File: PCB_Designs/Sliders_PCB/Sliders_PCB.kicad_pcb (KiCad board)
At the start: 2 copper layers, 67.1 x 80.5 mm, 6 parts, among them P1 CONN_01X06

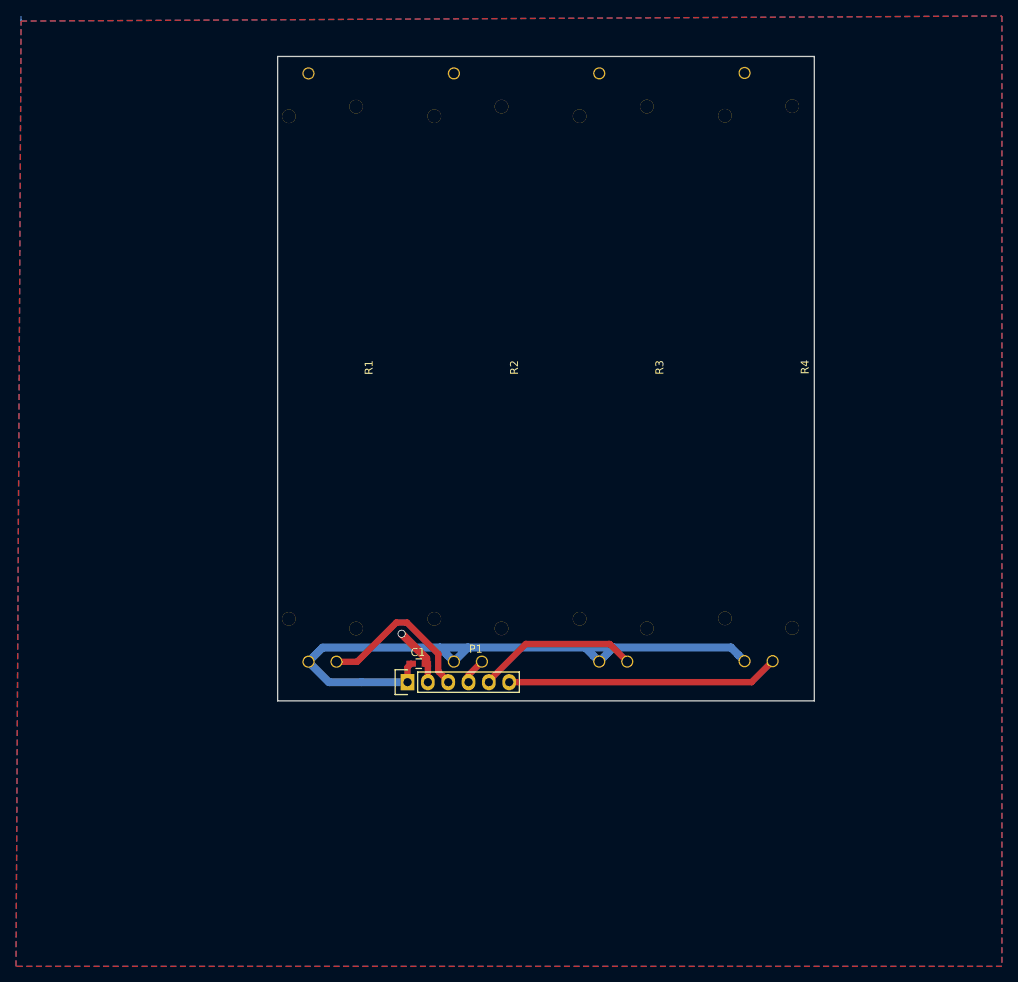
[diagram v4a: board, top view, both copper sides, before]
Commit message: Completed all Circuits for evaluation
* All board-to-board connectors now Multicomp 02X05
* Mounting holes for all PCB
* Vias at all groundpins
* Minor other changes
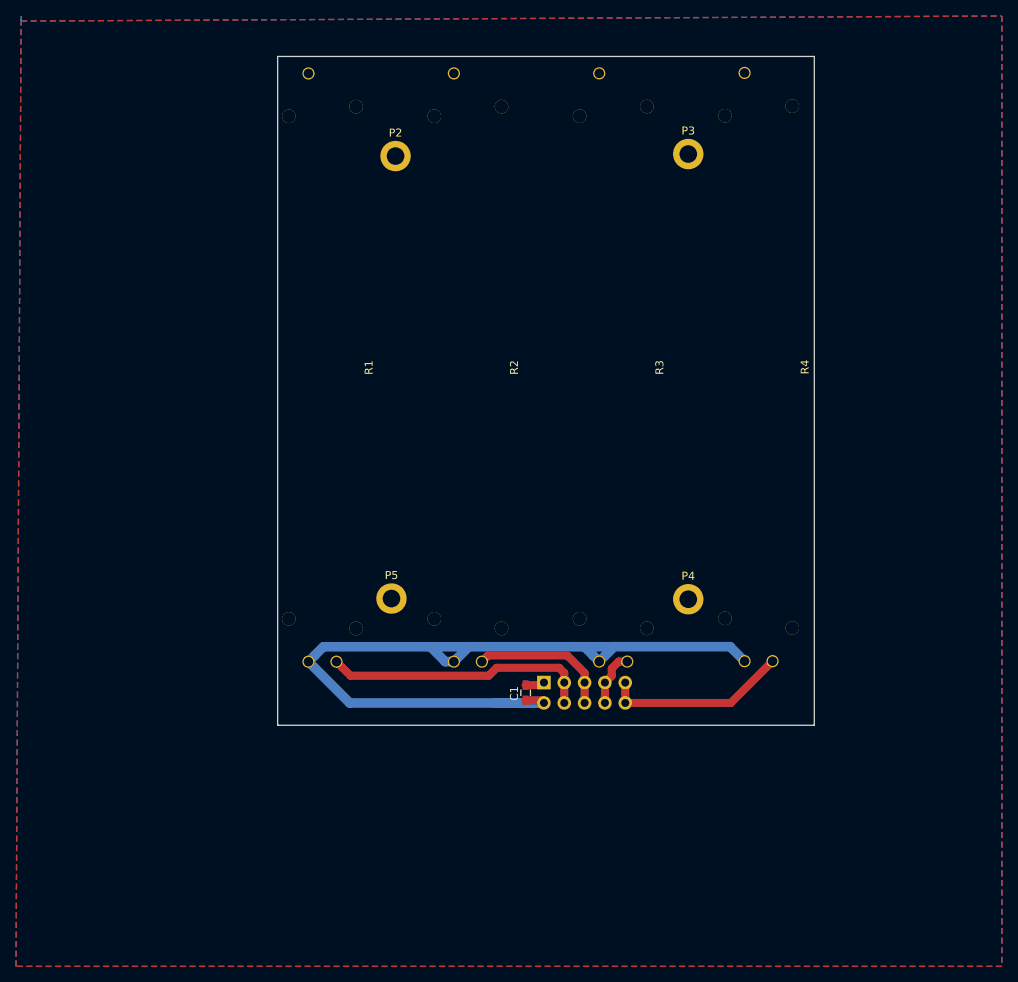
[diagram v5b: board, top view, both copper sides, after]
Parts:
- added P2: CONN_01X01, Mounting_Holes:MountingHole_2.2mm_M2_DIN965_Pad, F.Cu at (114.1, 38.5)
- added P3: CONN_01X01, Mounting_Holes:MountingHole_2.2mm_M2_DIN965_Pad, F.Cu at (150.7, 38.2)
- added P4: CONN_01X01, Mounting_Holes:MountingHole_2.2mm_M2_DIN965_Pad, F.Cu at (150.7, 93.8)
- added P5: CONN_01X01, Mounting_Holes:MountingHole_2.2mm_M2_DIN965_Pad, F.Cu at (113.6, 93.7)
- P1: value CONN_01X06 -> CONN_02X05; footprint Socket_Strips:Socket_Strip_Straight_1x06 -> Connectors_Multicomp:Multicomp_MC9A22-1034_2x05x2.54mm_Angled; moved to B.Cu
- moved P1 17.0 mm to (132.6, 104.2)
- moved C1 13.8 mm to (130.4, 105.5), turned to 90 degrees
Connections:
- P1 pad 1: /VDD -> /GND
- P1 pad 2: /GND -> /VDD
- P1 pad 4: Net-(P1-Pad4) -> Net-(P1-Pad3)
- P1 pad 6: Net-(P1-Pad6) -> Net-(P1-Pad5)
- R2 pad 2: Net-(P1-Pad4) -> Net-(P1-Pad5)
- R3 pad 2: Net-(P1-Pad5) -> Net-(P1-Pad7)
- R4 pad 2: Net-(P1-Pad6) -> Net-(P1-Pad10)
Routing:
- net Net-(P1-Pad6): track 34.0 -> 0.00 mm
- net /VDD: track 81.8 -> 107.7 mm
- net Net-(P1-Pad10): track 0.00 -> 23.1 mm
- net Net-(P1-Pad3): track 20.4 -> 33.6 mm
- net Net-(P1-Pad7): track 0.00 -> 6.95 mm
- net /GND: track 7.40 -> 2.42 mm, vias 1 -> 0
- net Net-(P1-Pad4): track 3.26 -> 0.00 mm
- net Net-(P1-Pad5): track 20.3 -> 17.8 mm
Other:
- board size 67.1 x 80.5 mm -> 67.1 x 83.6 mm

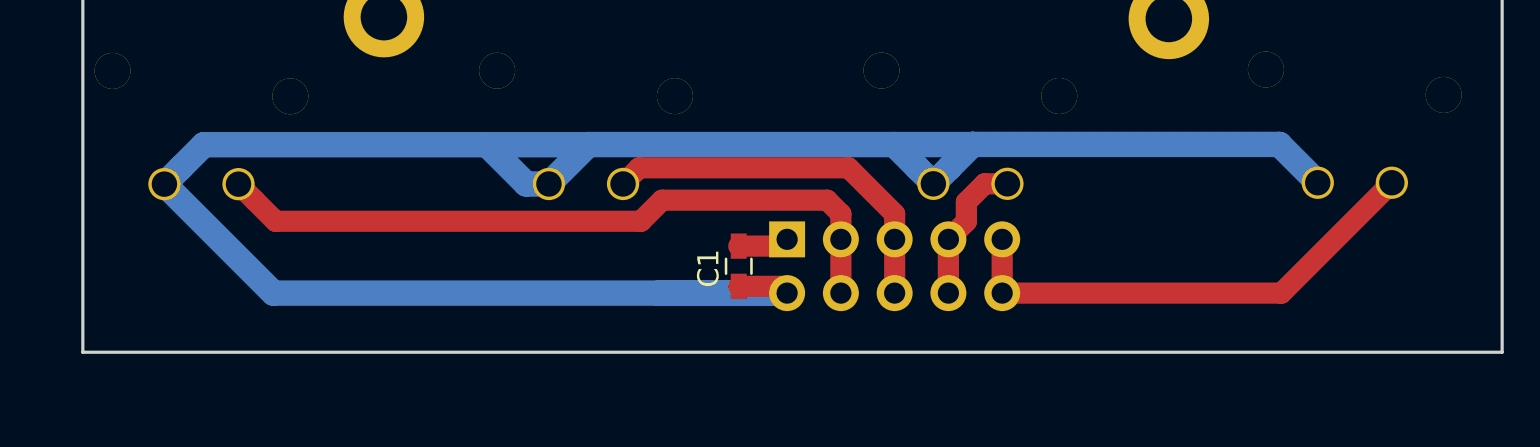
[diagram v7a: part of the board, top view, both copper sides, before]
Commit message: Edited Buttons and sliders for manufacturability
* All vias updated to 1.5 or 2 mm diameter
* Slight designchanges to get rid of drills close to edges in Buttons
* New Photomasks printed for Buttons and Sliders
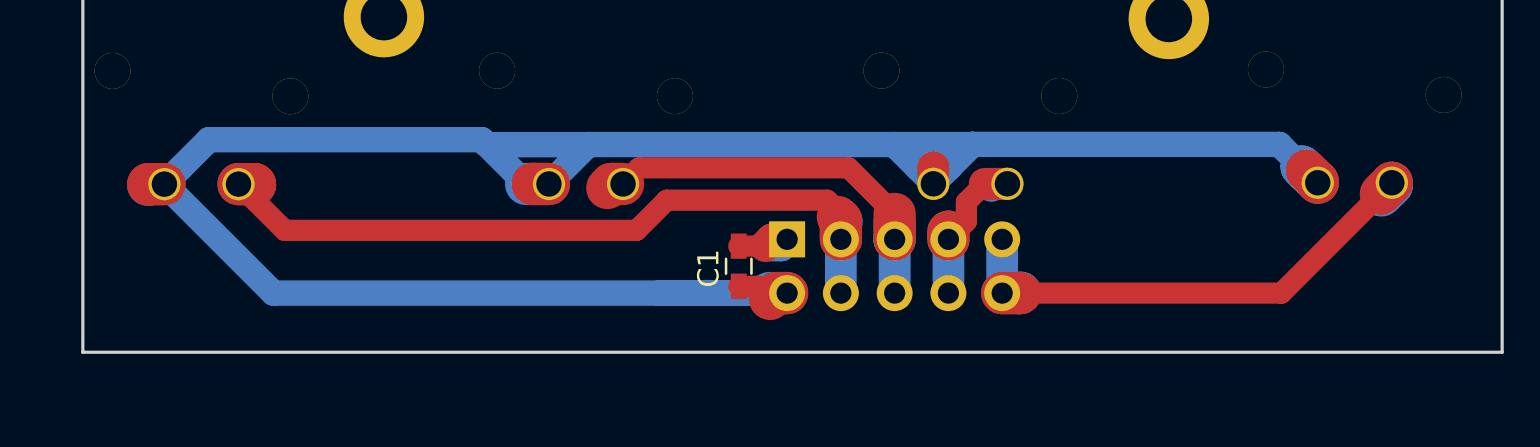
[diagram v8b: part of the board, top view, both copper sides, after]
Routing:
- net /VDD: track 107.7 -> 116.0 mm
- net Net-(P1-Pad3): track 33.6 -> 37.5 mm
- net Net-(P1-Pad10): track 23.1 -> 26.4 mm
- net Net-(P1-Pad5): track 17.8 -> 20.2 mm
- net Net-(P1-Pad7): track 6.95 -> 8.47 mm
- net /GND: track 2.42 -> 3.50 mm
